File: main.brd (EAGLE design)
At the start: 55.5 x 99.1 mm, 56 parts, among them CON1 451000, CON1_ 451000, CON2 451000, CON2_ 451000, IC1 MEGA8-AI, IC2 MC78M05ABDT, Q1 16MHz

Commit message: adding images of the current version
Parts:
- IC1: value MEGA8-AI -> ATMega88PA
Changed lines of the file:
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@@
 <layer number="14" name="Route14" color="1" fill="6" visible="no" active="no"/>
 <layer number="15" name="Route15" color="4" fill="6" visible="no" active="no"/>
-<layer number="16" name="Bottom" color="1" fill="1" visible="no" active="yes"/>
+<layer number="16" name="Bottom" color="1" fill="1" visible="yes" active="yes"/>
 <layer number="17" name="Pads" color="2" fill="1" visible="yes" active="yes"/>
 <layer number="18" name="Vias" color="2" fill="1" visible="yes" active="yes"/>
 <layer number="19" name="Unrouted" color="6" fill="1" visible="no" active="yes"/>
 <layer number="20" name="Dimension" color="15" fill="1" visible="yes" active="yes"/>
-<layer number="21" name="tPlace" color="7" fill="1" visible="no" active="yes"/>
-<layer number="22" name="bPlace" color="7" fill="1" visible="no" active="yes"/>
-<layer number="23" name="tOrigins" color="15" fill="1" visible="no" active="yes"/>
-<layer number="24" name="bOrigins" color="15" fill="1" visible="no" active="yes"/>
-<layer number="25" name="tNames" color="7" fill="1" visible="no" active="yes"/>
-<layer number="26" name="bNames" color="7" fill="1" visible="no" active="yes"/>
+<layer number="21" name="tPlace" color="7" fill="1" visible="yes" active="yes"/>
+<layer number="22" name="bPlace" color="7" fill="1" visible="yes" active="yes"/>
+<layer number="23" name="tOrigins" color="15" fill="1" visible="yes" active="yes"/>
+<layer number="24" name="bOrigins" color="15" fill="1" visible="yes" active="yes"/>
+<layer number="25" name="tNames" color="7" fill="1" visible="yes" active="yes"/>
+<layer number="26" name="bNames" color="7" fill="1" visible="yes" active="yes"/>
 <layer number="27" name="tValues" color="7" fill="1" visible="no" active="yes"/>
 <layer number="28" name="bValues" color="7" fill="1" visible="no" active="yes"/>
@@
 <layer number="43" name="vRestrict" color="2" fill="10" visible="no" active="yes"/>
 <layer number="44" name="Drills" color="7" fill="1" visible="no" active="yes"/>
-<layer number="45" name="Holes" color="7" fill="1" visible="no" active="yes"/>
+<layer number="45" name="Holes" color="7" fill="1" visible="yes" active="yes"/>
 <layer number="46" name="Milling" color="3" fill="1" visible="no" active="yes"/>
 <layer number="47" name="Measures" color="7" fill="1" visible="no" active="yes"/>
-<layer number="48" name="Document" color="7" fill="1" visible="no" active="yes"/>
-<layer number="49" name="Reference" color="7" fill="1" visible="no" active="yes"/>
+<layer number="48" name="Document" color="7" fill="1" visible="yes" active="yes"/>
+<layer number="49" name="Reference" color="7" fill="1" visible="yes" active="yes"/>
 <layer number="50" name="dxf" color="7" fill="1" visible="no" active="no"/>
-<layer number="51" name="tDocu" color="7" fill="1" visible="no" active="yes"/>
-<layer number="52" name="bDocu" color="7" fill="1" visible="no" active="yes"/>
+<layer number="51" name="tDocu" color="7" fill="1" visible="yes" active="yes"/>
+<layer number="52" name="bDocu" color="7" fill="1" visible="yes" active="yes"/>
 <layer number="53" name="tGND_GNDA" color="7" fill="9" visible="no" active="no"/>
 <layer number="54" name="bGND_GNDA" color="1" fill="9" visible="no" active="no"/>
@@
 <attribute name="OC_FARNELL" value="unknown" x="100.33" y="-33.655" size="1.778" layer="27" display="off"/>
 </element>
-<element name="IC1" library="avr-7" package="TQFP32-08" value="MEGA8-AI" x="34.29" y="36.83" rot="R270"/>
+<element name="IC1" library="avr-7" package="TQFP32-08" value="ATMega88PA" x="34.29" y="36.83" rot="R270"/>
 <element name="JP1" library="avr-7" package="AVR-ISP-10" value="AVR-ISP-10" x="27.94" y="24.13" rot="R180"/>
 <element name="C5" library="rcl" package="C0805" value="100n" x="34.925" y="43.18"/>

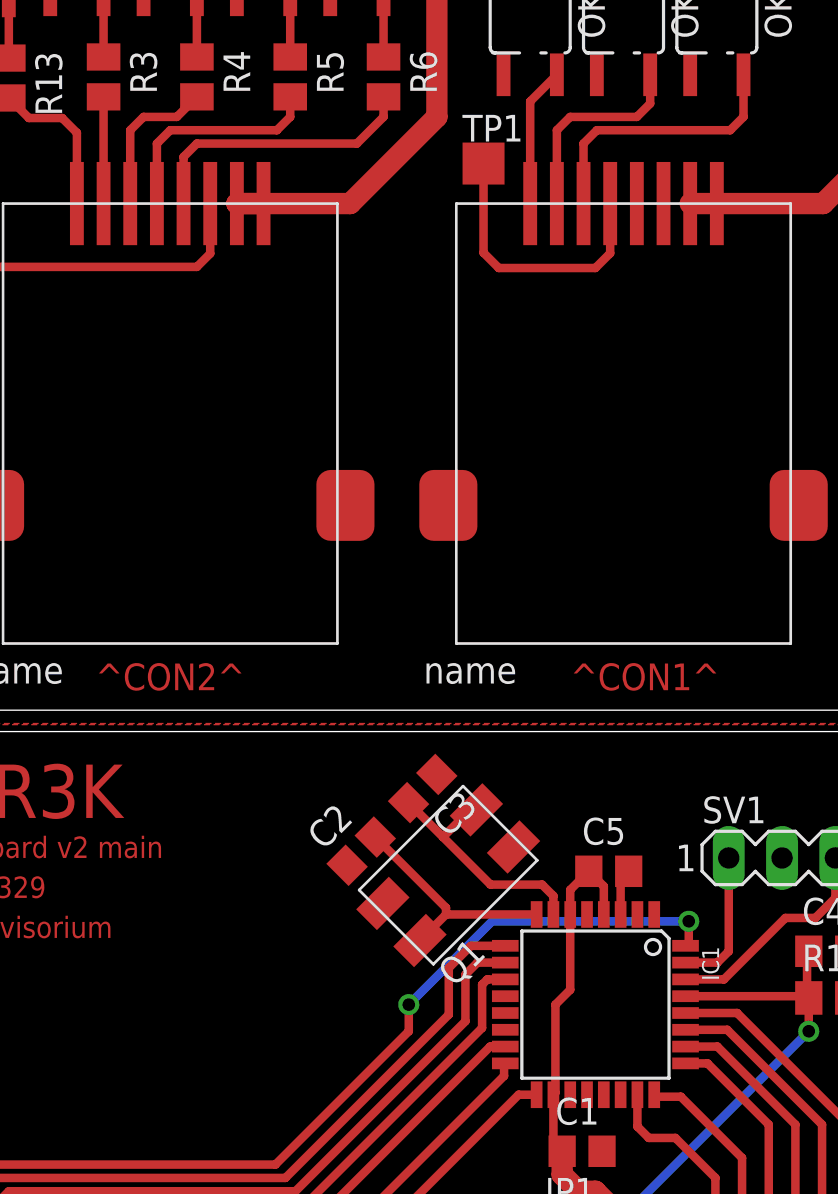
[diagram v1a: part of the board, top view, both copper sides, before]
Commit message: Optokoppler für Daymode => Optokoppler für Datenleitung
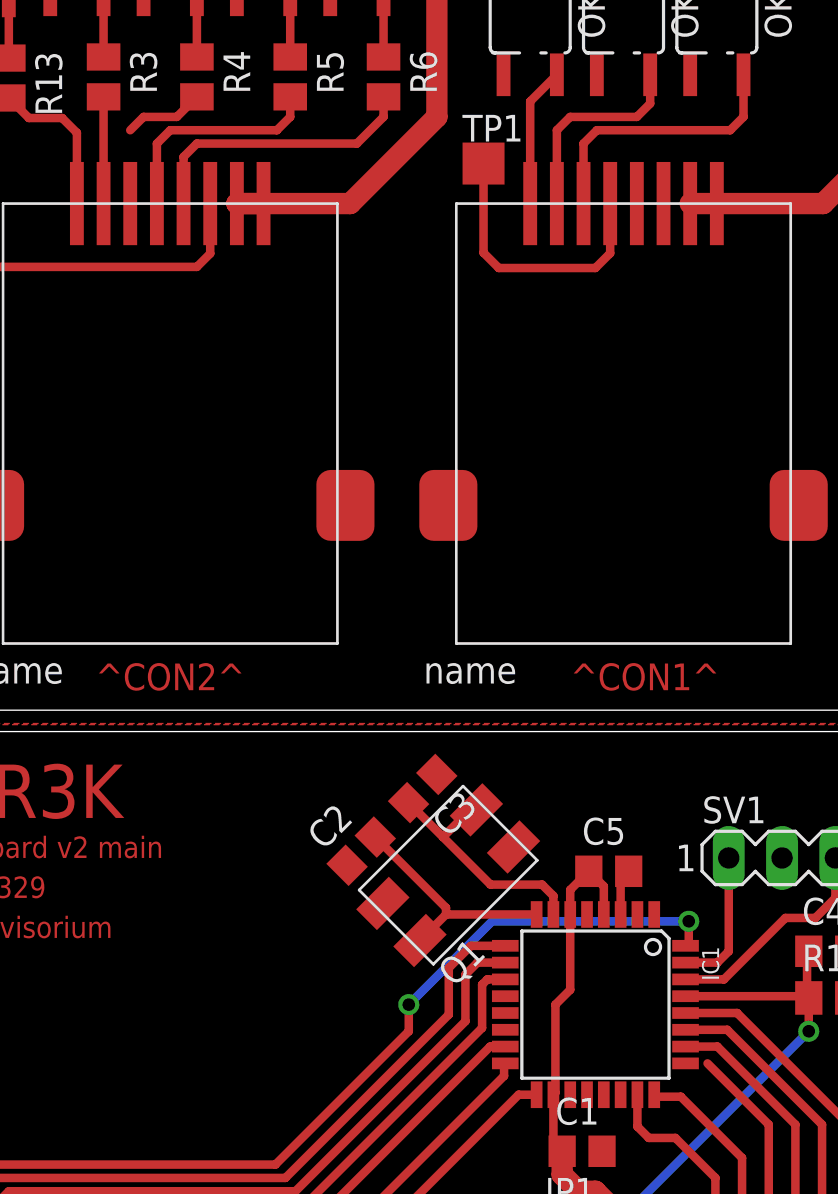
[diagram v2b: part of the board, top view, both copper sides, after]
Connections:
- net DOOR_DAYMODE renamed DOOR_DATA
- net DOOR_DAYMODE_+ renamed DOOR_DATA_+
- net DOOR_DAYMODE_- renamed DOOR_DATA_-
- net _DOOR_DAYMODE renamed _DOOR_DATA
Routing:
- net _DOOR_DATA: track 7.33 -> 3.83 mm
- net DOOR_DATA: track 12.8 -> 11.7 mm
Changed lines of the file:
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@@
 <wire x1="37.09" y1="32.4425" x2="37.09" y2="32.5374" width="0.4064" layer="1"/>
-</signal>
-<signal name="DOOR_DAYMODE">
-<contactref element="IC1" pad="25"/>
-<contactref element="CON2" pad="3"/>
-<wire x1="42.545" y1="23.495" x2="42.545" y2="31.115" width="0.4064" layer="1"/>
-<wire x1="42.545" y1="31.115" x2="39.63" y2="34.03" width="0.4064" layer="1"/>
-<wire x1="38.5826" y1="34.03" x2="39.63" y2="34.03" width="0.4064" layer="1"/>
 </signal>
 <signal name="LED_IN">
@@
 <wire x1="10.86353125" y1="95.620459375" x2="8.95853125" y2="97.525459375" width="0.4064" layer="1"/>
 </signal>
-<signal name="DOOR_DAYMODE_+">
+<signal name="DOOR_DATA_+">
 <contactref element="OK3" pad="6"/>
 <contactref element="TP11" pad="TP"/>
@@
 <wire x1="12.76853125" y1="93.715459375" x2="13.40353125" y2="94.350459375" width="0.4064" layer="1"/>
 </signal>
-<signal name="DOOR_DAYMODE_-">
+<signal name="DOOR_DATA_-">
 <contactref element="OK3" pad="4"/>
 <contactref element="TP12" pad="TP"/>
@@
 <wire x1="13.40353125" y1="74.982959375" x2="13.40353125" y2="77.840459375" width="0.4064" layer="1"/>
 </signal>
-<signal name="_DOOR_DAYMODE">
-<contactref element="R4" pad="2"/>
-<contactref element="CON2_" pad="3"/>
-<wire x1="12.13353125" y1="78.475459375" x2="12.76853125" y2="79.110459375" width="0.4064" layer="1"/>
-<wire x1="12.76853125" y1="79.110459375" x2="14.35353125" y2="79.110459375" width="0.4064" layer="1"/>
-<wire x1="14.35353125" y1="79.110459375" x2="15.30853125" y2="80.065459375" width="0.4064" layer="1"/>
-<wire x1="12.13353125" y1="74.982959375" x2="12.13353125" y2="78.475459375" width="0.4064" layer="1"/>
-</signal>
 <signal name="_DOOR_OPEN">
 <contactref element="R3" pad="2"/>
@@
 <wire x1="6.35" y1="81.9125" x2="6.35" y2="84.8741" width="0.4064" layer="1"/>
 </signal>
+<signal name="DOOR_DATA">
+<contactref element="IC1" pad="25"/>
+<contactref element="CON2" pad="3"/>
+<wire x1="42.545" y1="23.495" x2="42.545" y2="31.115" width="0.4064" layer="1"/>
+<wire x1="42.545" y1="31.115" x2="39.63" y2="34.03" width="0.4064" layer="1"/>
+<wire x1="39.63" y1="34.03" x2="38.5826" y2="34.03" width="0" layer="19" extent="1-1"/>
+</signal>
+<signal name="_DOOR_DATA">
+<contactref element="CON2_" pad="3"/>
+<contactref element="R4" pad="2"/>
+<wire x1="12.13353125" y1="78.475459375" x2="12.76853125" y2="79.110459375" width="0.4064" layer="1"/>
+<wire x1="12.76853125" y1="79.110459375" x2="14.35353125" y2="79.110459375" width="0.4064" layer="1"/>
+<wire x1="14.35353125" y1="79.110459375" x2="15.30853125" y2="80.065459375" width="0.4064" layer="1"/>
+<wire x1="12.13353125" y1="74.982959375" x2="12.13353125" y2="78.475459375" width="0" layer="19" extent="1-1"/>
+</signal>
 </signals>
